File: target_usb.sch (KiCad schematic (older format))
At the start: 22 parts, among them J2 USB_C_Receptacle, U1 USB6B1, U2 USB6B1, U3 FUSB302BMPX, U4 USB6B1, U5 USB6B1

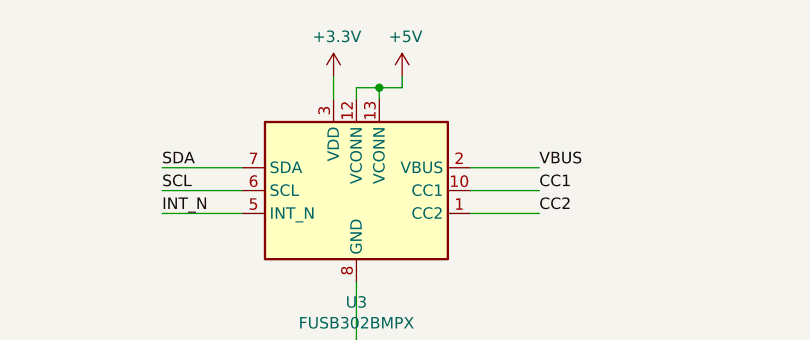
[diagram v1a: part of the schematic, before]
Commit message: Add initial power design
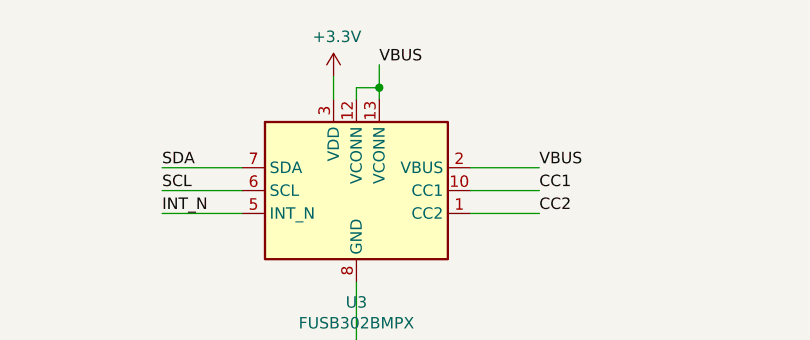
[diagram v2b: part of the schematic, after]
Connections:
- net +5V is gone; now on net VBUS: U3.12 (VCONN), U3.13 (VCONN)
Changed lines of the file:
@@
-	1    0    0    -1
-$EndComp
-$Comp
-L power:+5V #PWR010
-U 1 1 61A564F1
-P 5800 1150
-F 0 "#PWR010" H 5800 1000 50  0001 C CNN
-F 1 "+5V" H 5815 1323 50  0000 C CNN
-F 2 "" H 5800 1150 50  0001 C CNN
-F 3 "" H 5800 1150 50  0001 C CNN
-	1    5800 1150
 	1    0    0    -1
 $EndComp
@@
 Wire Wire Line
 	5500 1250 5500 1150
-Wire Wire Line
-	5800 1150 5800 1200
-Wire Wire Line
-	5800 1200 5700 1200
-Connection ~ 5700 1200
 Text Label 6400 1550 0    50   ~ 0
 VBUS
@@
 Wire Wire Line
 	5600 2050 5600 2300
+Text Label 5700 1100 0    50   ~ 0
+VBUS
+Wire Wire Line
+	5700 1100 5700 1200
+Connection ~ 5700 1200
 $EndSCHEMATC

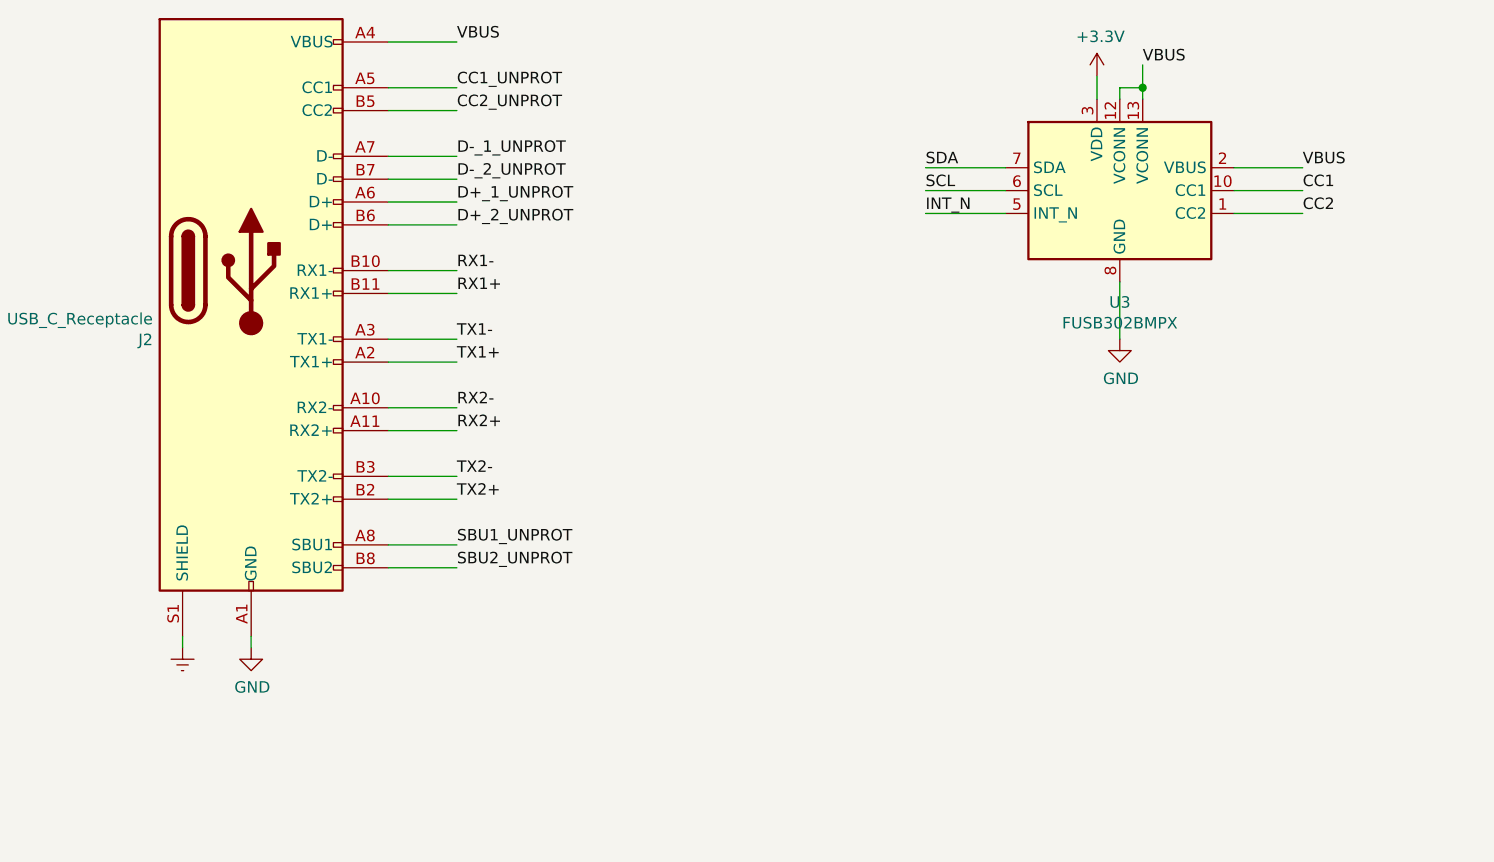
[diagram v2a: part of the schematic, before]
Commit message: Supply caps, initial signal states and headers
  * Added bulk supply caps.
  * Set initial control signal states via resistors.
  * Add debug headers.
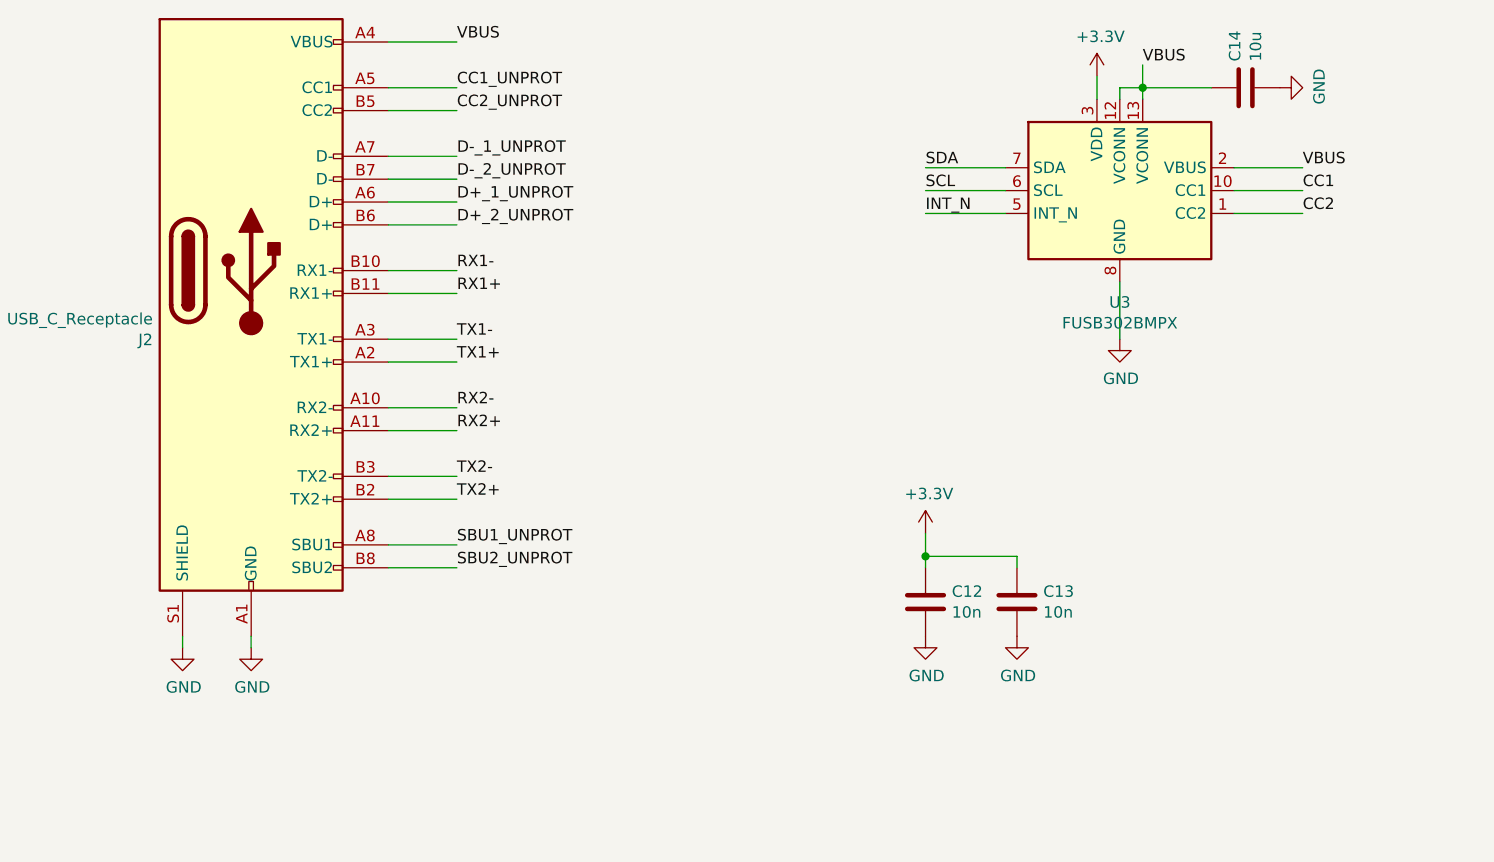
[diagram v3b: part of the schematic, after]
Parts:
- added C12, C13: 10n, symbol Device:C
- added C14: 10u, symbol Device:C
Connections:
- net Earth is gone; now on net GND: J2.S1 (SHIELD)
- net +3V3: now also C12.1, C13.1
- net GND: now also C12.2, C13.2, C14.2
- net VBUS: now also C14.1
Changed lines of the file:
@@
-	1    0    0    -1
-$EndComp
-$Comp
-L power:Earth #PWR02
-U 1 1 619E23EC
-P 1500 3650
-F 0 "#PWR02" H 1500 3400 50  0001 C CNN
-F 1 "Earth" H 1500 3500 50  0001 C CNN
-F 2 "" H 1500 3650 50  0001 C CNN
-F 3 "~" H 1500 3650 50  0001 C CNN
-	1    1500 3650
 	1    0    0    -1
 $EndComp
@@
 	5700 1100 5700 1200
 Connection ~ 5700 1200
+$Comp
+L Device:C C12
+U 1 1 61B7E17E
+P 4750 3450
+F 0 "C12" H 4865 3496 50  0000 L CNN
+F 1 "10n" H 4865 3405 50  0000 L CNN
+F 2 "" H 4788 3300 50  0001 C CNN
+F 3 "~" H 4750 3450 50  0001 C CNN
+	1    4750 3450
+	1    0    0    -1
+$EndComp
+$Comp
+L power:GND #PWR0112
+U 1 1 61B7E184
+P 4750 3600
+F 0 "#PWR0112" H 4750 3350 50  0001 C CNN
+F 1 "GND" H 4755 3427 50  0000 C CNN
+F 2 "" H 4750 3600 50  0001 C CNN
+F 3 "" H 4750 3600 50  0001 C CNN
+	1    4750 3600
+	1    0    0    -1
+$EndComp
+$Comp
+L power:+3.3V #PWR0131
+U 1 1 61B7E18A
+P 4750 3150
+F 0 "#PWR0131" H 4750 3000 50  0001 C CNN
+F 1 "+3.3V" H 4765 3323 50  0000 C CNN
+F 2 "" H 4750 3150 50  0001 C CNN
+F 3 "" H 4750 3150 50  0001 C CNN
+	1    4750 3150
+	1    0    0    -1
+$EndComp
+$Comp
+L Device:C C13
+U 1 1 61B7E190
+P 5150 3450
+F 0 "C13" H 5265 3496 50  0000 L CNN
+F 1 "10n" H 5265 3405 50  0000 L CNN
+F 2 "" H 5188 3300 50  0001 C CNN
+F 3 "~" H 5150 3450 50  0001 C CNN
+	1    5150 3450
+	1    0    0    -1
+$EndComp
+$Comp
+L power:GND #PWR0132
+U 1 1 61B7E196
+P 5150 3600
+F 0 "#PWR0132" H 5150 3350 50  0001 C CNN
+F 1 "GND" H 5155 3427 50  0000 C CNN
+F 2 "" H 5150 3600 50  0001 C CNN
+F 3 "" H 5150 3600 50  0001 C CNN
+	1    5150 3600
+	1    0    0    -1
+$EndComp
+Wire Wire Line
+	4750 3250 4750 3150
+Wire Wire Line
+	4750 3250 4750 3300
+Connection ~ 4750 3250
+Wire Wire Line
+	5150 3250 5150 3300
+Wire Wire Line
+	5150 3250 4750 3250
+$Comp
+L Device:C C?
+U 1 1 61B831A1
+P 6150 1200
+AR Path="/61EE6DE0/61B831A1" Ref="C?"  Part="1"
+AR Path="/619A9DB6/61B831A1" Ref="C14"  Part="1"
+F 0 "C14" H 6265 1246 50  0000 L CNN
+F 1 "10u" H 6265 1155 50  0000 L CNN
+F 2 "" H 6188 1050 50  0001 C CNN
+F 3 "~" H 6150 1200 50  0001 C CNN
+	1    6150 1200
+	0    -1   -1   0
+$EndComp
+$Comp
+L power:GND #PWR0133
+U 1 1 61B8744B
+P 6300 1200
+F 0 "#PWR0133" H 6300 950 50  0001 C CNN
+F 1 "GND" H 6305 1027 50  0000 C CNN
+F 2 "" H 6300 1200 50  0001 C CNN
+F 3 "" H 6300 1200 50  0001 C CNN
+	1    6300 1200
+	0    -1   -1   0
+$EndComp
+Wire Wire Line
+	6000 1200 5700 1200
+$Comp
+L power:GND #PWR0191
+U 1 1 61AC9F81
+P 1500 3650
+F 0 "#PWR0191" H 1500 3400 50  0001 C CNN
+F 1 "GND" H 1505 3477 50  0000 C CNN
+F 2 "" H 1500 3650 50  0001 C CNN
+F 3 "" H 1500 3650 50  0001 C CNN
+	1    1500 3650
+	1    0    0    -1
+$EndComp
 $EndSCHEMATC

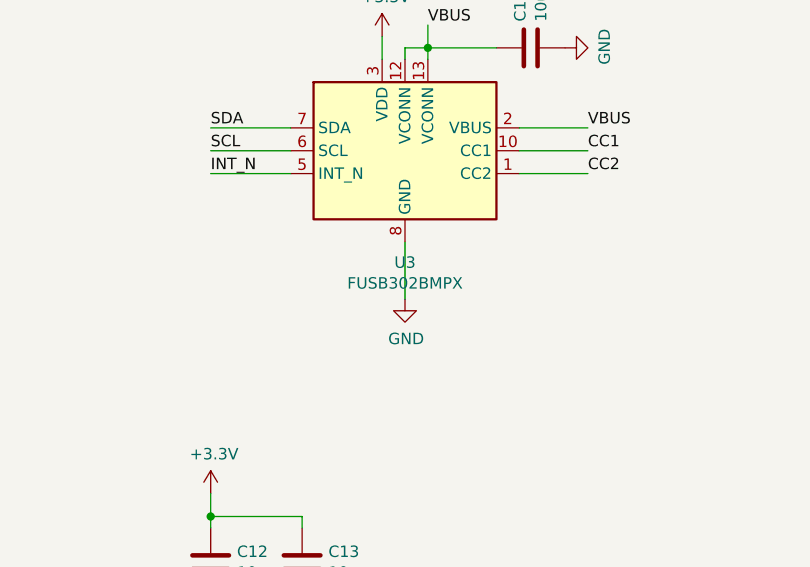
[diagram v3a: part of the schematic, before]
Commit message: Replace MCU by something available in distributors
Given the current chip shortage the STM32F0 was not available from
JLCPCB. This one (STM32F411CE) is available in large quantities from
JLCPCB. Despite being much more powerful than the F0, it is still in the
price range and actually cheaper than the STM32F103C8T6... which I don't
understand...
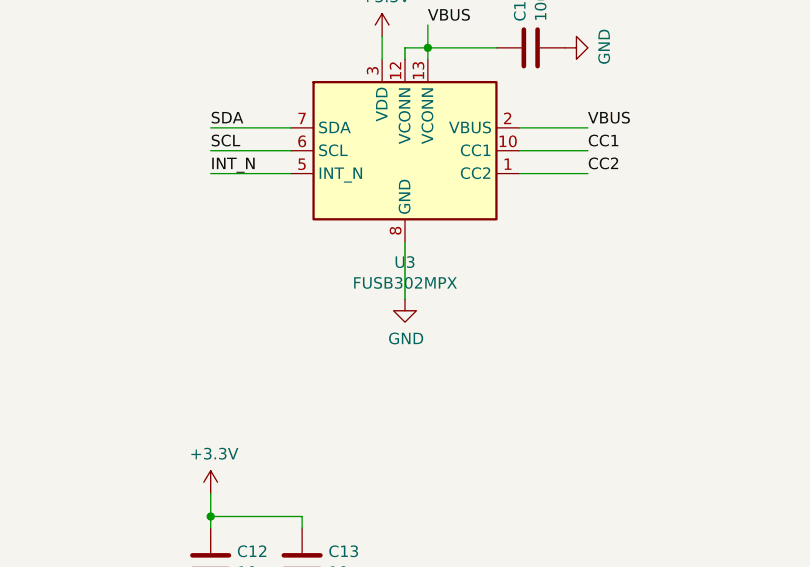
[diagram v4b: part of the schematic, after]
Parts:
- U1, U2, U4, U5: LCSC (none) -> C10508
- U3: value FUSB302BMPX -> FUSB302MPX; LCSC (none) -> C442699
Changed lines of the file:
@@
 AR Path="/619A9DB6/619F286D" Ref="U3"  Part="1"
 F 0 "U3" H 5600 1161 50  0000 C CNN
-F 1 "FUSB302BMPX" H 5600 1070 50  0000 C CNN
+F 1 "FUSB302MPX" H 5600 1070 50  0000 C CNN
 F 2 "Package_DFN_QFN:WQFN-14-1EP_2.5x2.5mm_P0.5mm_EP1.45x1.45mm" H 5600 1150 50  0001 C CNN
 F 3 "http://www.onsemi.com/pub/Collateral/FUSB302B-D.PDF" H 5700 1250 50  0001 C CNN
+F 4 "C442699" H 5600 1650 50  0001 C CNN "LCSC"
 	1    5600 1650
 	1    0    0    -1
@@
 F 2 "Package_SO:SOIC-8_3.9x4.9mm_P1.27mm" H 3550 5400 50  0001 C CNN
 F 3 "http://www.st.com/content/ccc/resource/technical/document/datasheet/3e/ec/b2/54/b2/76/47/90/CD00001361.pdf/files/CD00001361.pdf/jcr:content/translations/en.CD00001361.pdf" H 2600 5300 50  0001 C CNN
+F 4 "C10508" H 3550 5400 50  0001 C CNN "LCSC"
 	1    3550 5400
 	1    0    0    -1
@@
 F 2 "Package_SO:SOIC-8_3.9x4.9mm_P1.27mm" H 5600 5400 50  0001 C CNN
 F 3 "http://www.st.com/content/ccc/resource/technical/document/datasheet/3e/ec/b2/54/b2/76/47/90/CD00001361.pdf/files/CD00001361.pdf/jcr:content/translations/en.CD00001361.pdf" H 4650 5300 50  0001 C CNN
+F 4 "C10508" H 5600 5400 50  0001 C CNN "LCSC"
 	1    5600 5400
 	1    0    0    -1
@@
 F 2 "Package_SO:SOIC-8_3.9x4.9mm_P1.27mm" H 5600 6700 50  0001 C CNN
 F 3 "http://www.st.com/content/ccc/resource/technical/document/datasheet/3e/ec/b2/54/b2/76/47/90/CD00001361.pdf/files/CD00001361.pdf/jcr:content/translations/en.CD00001361.pdf" H 4650 6600 50  0001 C CNN
+F 4 "C10508" H 5600 6700 50  0001 C CNN "LCSC"
 	1    5600 6700
 	1    0    0    -1
@@
 F 2 "Package_SO:SOIC-8_3.9x4.9mm_P1.27mm" H 3550 6700 50  0001 C CNN
 F 3 "http://www.st.com/content/ccc/resource/technical/document/datasheet/3e/ec/b2/54/b2/76/47/90/CD00001361.pdf/files/CD00001361.pdf/jcr:content/translations/en.CD00001361.pdf" H 2600 6600 50  0001 C CNN
+F 4 "C10508" H 3550 6700 50  0001 C CNN "LCSC"
 	1    3550 6700
 	1    0    0    -1
